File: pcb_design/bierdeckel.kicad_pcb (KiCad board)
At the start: 2 copper layers, 93 x 93 mm, 72 parts, among them IC1 HSFPAR004A, J1 Pogo, J2 Pogo, J6 USB-TYPE-C-020, Q1 BSS123, Q2 SP20P18T1, Q3 BSS123, SW1 PTS526 SK15 SMTR2 LFS, SW2 PTS526 SK15 SMTR2 LFS, SW3 PTS526 SK15 SMTR2 LFS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

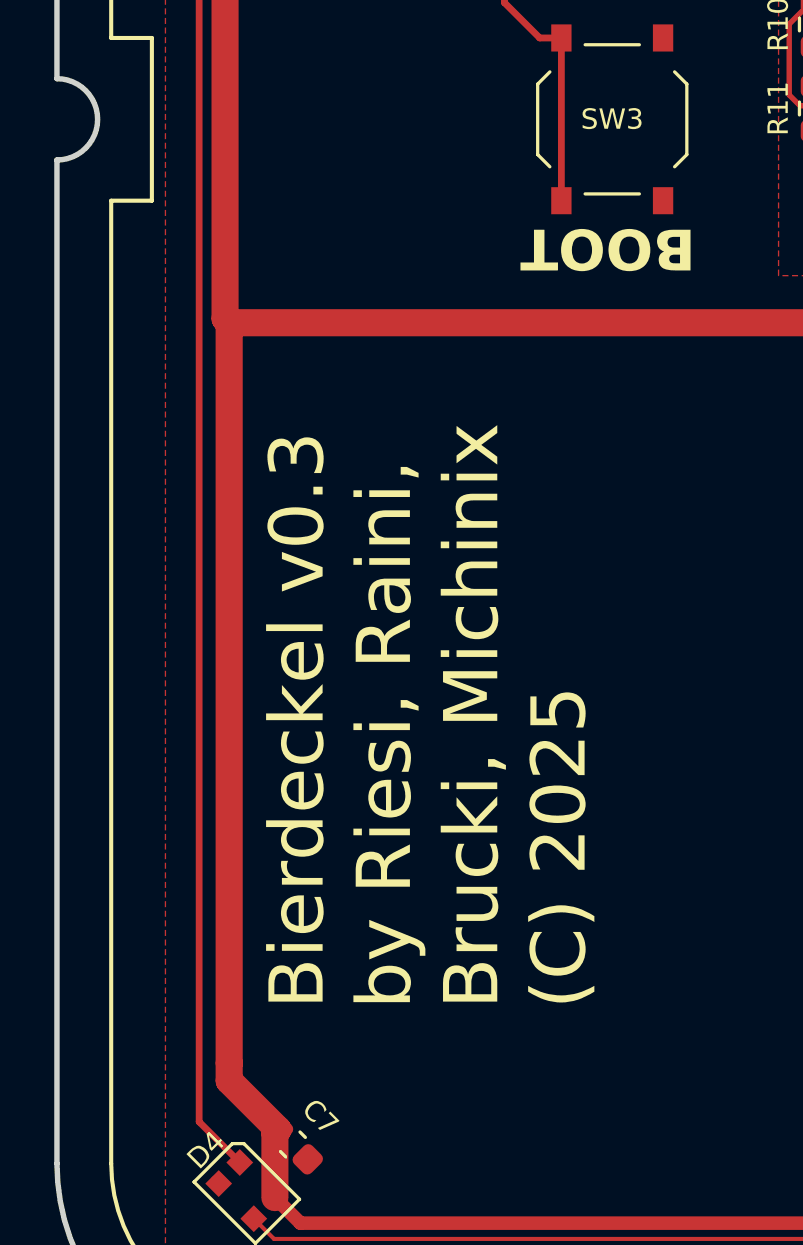
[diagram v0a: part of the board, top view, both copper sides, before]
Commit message: add license to PCB silkscreen
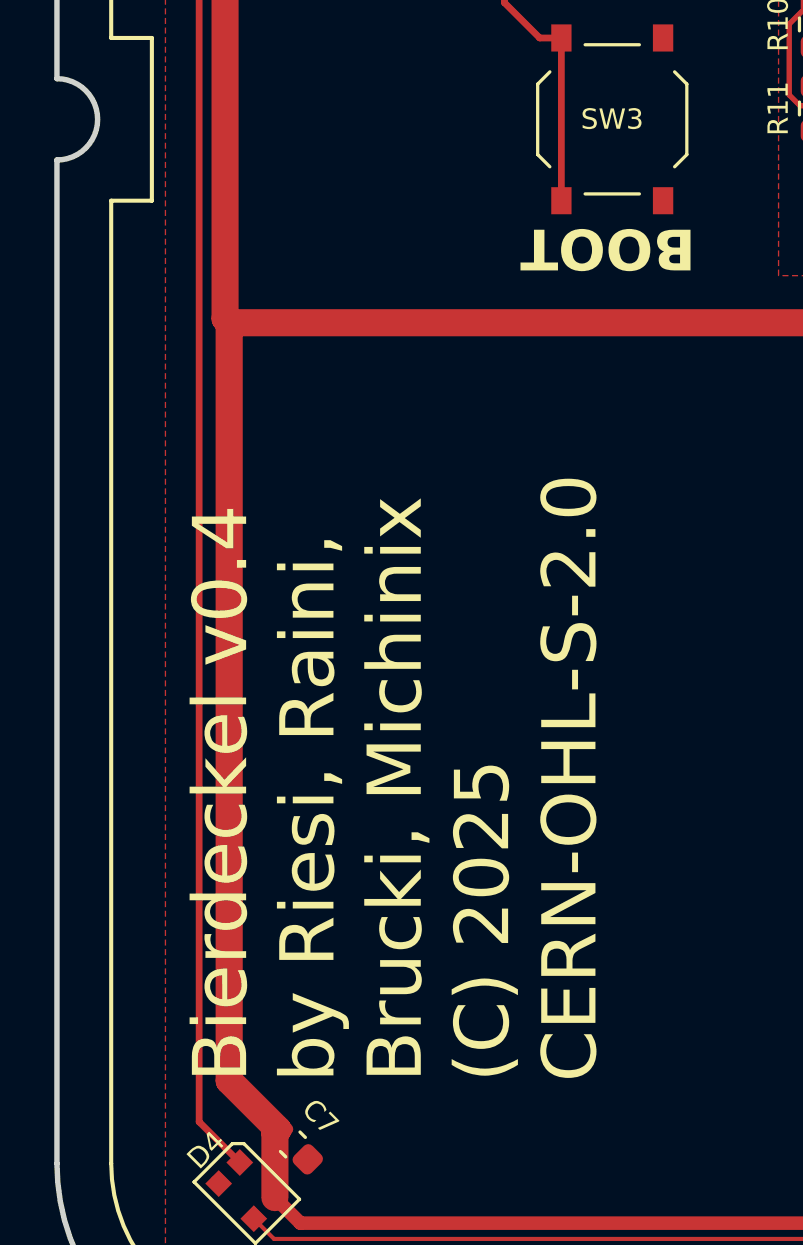
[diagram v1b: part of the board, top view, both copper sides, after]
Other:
- board text added: "Bierdeckel v${REVISION} by Riesi, Raini, Brucki, Michinix (C) 2025 ${COMMENT9}"
- board text removed: "Bierdeckel v0.3 by Riesi, Raini, Brucki, Michinix (C) 2025"
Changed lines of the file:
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@@
 		(comment 2 "SPDX-FileCopyrightText: 2023-2025 Stefan Riesenberger <stefan.riesenberger@gmail.com>")
 		(comment 4 "AISLER Project ID: MNJWCNXA")
+		(comment 9 "CERN-OHL-S-2.0")
 	)
 	(layers
@@
 		)
 	)
-	(gr_text "Bierdeckel v0.3\nby Riesi, Raini,\nBrucki, Michinix\n(C) 2025"
-		(at 119.7 129.3 90)
+	(gr_text "Bierdeckel v${REVISION}\nby Riesi, Raini,\nBrucki, Michinix\n(C) 2025\n${COMMENT9}"
+		(at 120.1 132 90)
 		(layer "F.SilkS")
 		(effects
